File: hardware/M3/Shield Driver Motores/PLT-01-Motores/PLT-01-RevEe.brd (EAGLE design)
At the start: 68.6 x 53.6 mm, 14 parts

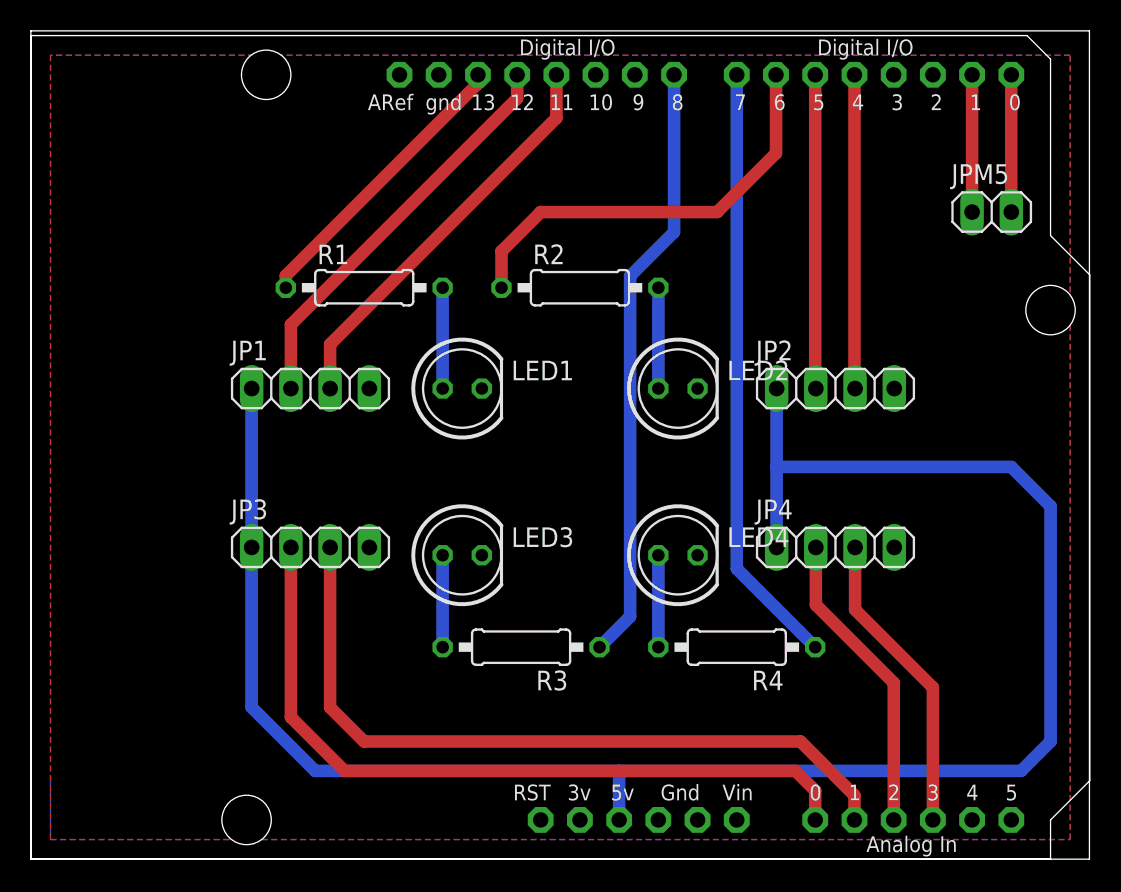
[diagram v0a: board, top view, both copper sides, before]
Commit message: Se arreglan clearences de algunas placas
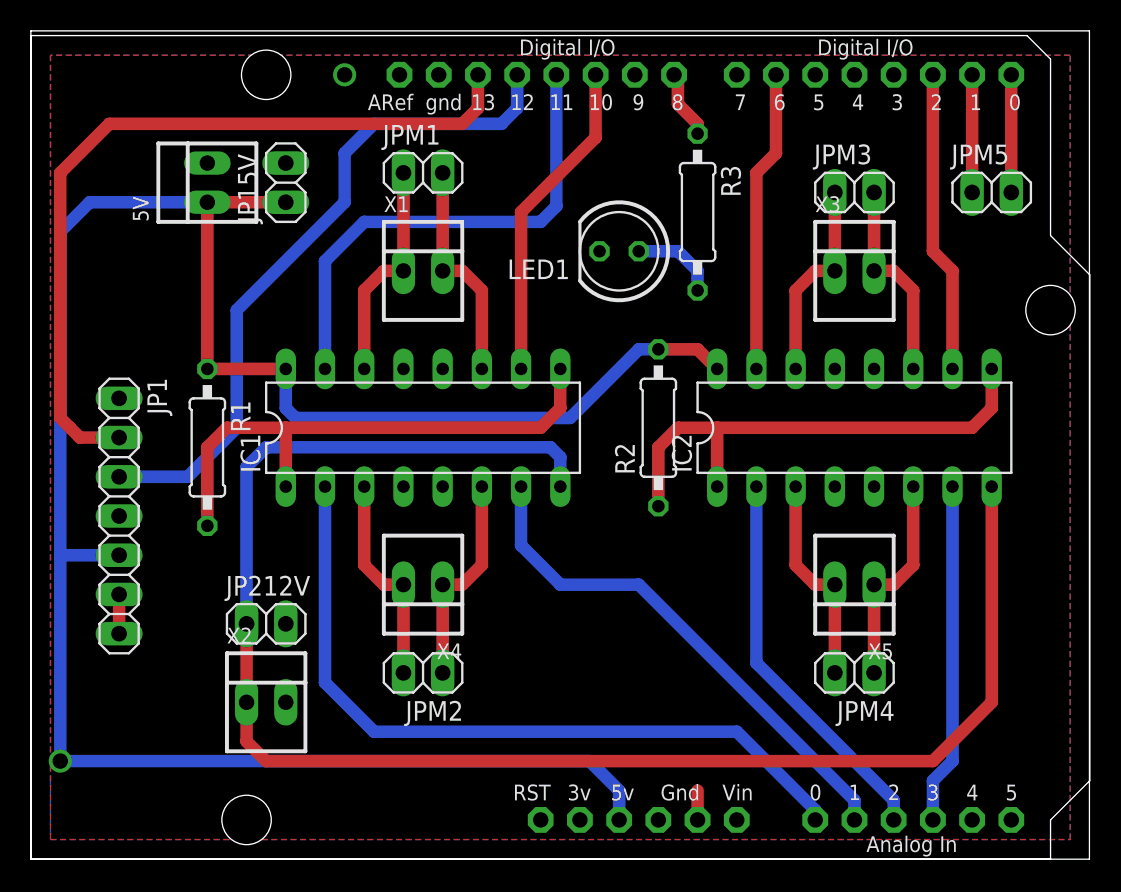
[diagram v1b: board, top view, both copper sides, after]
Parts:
- removed JP2, JP3, JP4: (no value), pinhead:1X04
- removed LED2, LED3, LED4: (no value), led:LED5MM
- removed R4: (no value), resistor:0207/10
- added 5V, X1, X2, X3, X4, X5: 22-23-2021, con-molex:22-23-2021
- added IC1, IC2: L293D, st-microelectronics:DIL16
- added JP15V, JP212V, JPM1, JPM2, JPM3, JPM4: (no value), pinhead:1X02
- JP1: device pinhead:1X04 -> pinhead:1X07
- moved R3 30.4 mm to (52.1, 45.7), turned to 270 degrees
- moved JP1 14.9 mm to (14.6, 26.0), turned to 270 degrees
- moved R1 14.5 mm to (20.3, 30.5), turned to 270 degrees
- moved LED1 13.5 mm to (47.0, 43.2), turned to 180 degrees
- moved R2 10.4 mm to (49.5, 31.8), turned to 90 degrees
- moved JPM5 1.27 mm to (71.1, 47.0)
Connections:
- removed net N$10 (its old number): R1.1, U$1.D13
- removed net N$14: LED4.A, R4.2
- removed net N$15: JP3.2, U$1.A0
- removed net N$16: LED3.A, R3.2
- removed net N$17: JP3.3, U$1.A1
- new net 1A1: IC1.2, U$1.A0
- new net 1A2: IC2.2, U$1.A2
- new net 2A1: IC1.7, U$1.A1
- new net 2A2: IC2.7, U$1.A3
- new net 3A1: IC1.10, U$1.D10
- new net 3A2: IC2.10, U$1.D2
- new net 4A1: IC1.15, U$1.D11
- new net 4A2: IC2.15, U$1.D6
- new net GND4: IC2.12
- new net N$2: IC1.6, JPM2.1, X4.1
- new net N$7: IC1.14, JPM1.1, X1.1
- new net RXBT: JP1.2, U$1.D13
- new net TXBT: JP1.3, U$1.D12
- new net VCC2: IC1.8, IC2.8, JP212V.1, X2.1
- net 5V: now also 5V.1, IC1.16, IC2.16, JP1.5, JP15V.1, R1.1, R2.2; no longer JP1.1, JP2.1, JP3.1, JP4.1
- net GND: now also 5V.2, IC1.12, IC1.13, IC1.4, IC1.5, IC2.13, IC2.4, IC2.5, JP15V.2, JP212V.2, X2.2; no longer JP2.4, JP3.4, JP4.4, LED2.K, LED3.K, LED4.K
- net N$1: now also IC1.3, JPM2.2, X4.2; no longer JP4.3, U$1.A3
- net N$11: now also IC1.1, IC1.9, R1.2; no longer LED2.A, R2.2
- net N$12: now also R3.2; no longer R1.2
- net N$13: now also JP1.6, JP1.7; no longer R2.1, U$1.D6
- net N$3: now also IC2.3, JPM4.2, X5.2; no longer R4.1, U$1.D7
- net N$4: now also IC2.6, JPM4.1, X5.1; no longer JP2.3, U$1.D4
- net N$5: now also IC2.14, JPM3.1, X3.1; no longer JP2.2, U$1.D5
- net N$6: now also IC2.11, JPM3.2, X3.2; no longer JP4.2, U$1.A2
- net N$8: now also IC1.11, JPM1.2, X1.2; no longer JP1.3, U$1.D11
- net N$9: now also IC2.1, IC2.9, R2.1; no longer JP1.2, U$1.D12
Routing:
- net VCC2: track 0.00 -> 105.1 mm
- net RXBT: track 0.00 -> 51.2 mm
- net N$15: track 48.8 -> 0.00 mm
- net 1A1: track 0.00 -> 48.5 mm
- net N$17: track 48.3 -> 0.00 mm
- net TXBT: track 0.00 -> 44.2 mm
- net N$10: track 39.1 -> 4.44 mm
- net 2A1: track 0.00 -> 33.5 mm
- net 4A1: track 0.00 -> 32.0 mm
- net N$11: track 6.53 -> 35.3 mm
- net N$3: track 39.2 -> 13.9 mm
- net N$13: track 27.9 -> 2.54 mm
- net 1A2: track 0.00 -> 25.3 mm
- net 2A2: track 0.00 -> 22.1 mm
- net 3A1: track 0.00 -> 21.0 mm
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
